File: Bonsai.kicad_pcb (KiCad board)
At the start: 2 copper layers, 348.5 x 165.6 mm, 202 parts, among them J1 AVR-ISP-6, U1 ATmega32A-PU, Y1 Crystal

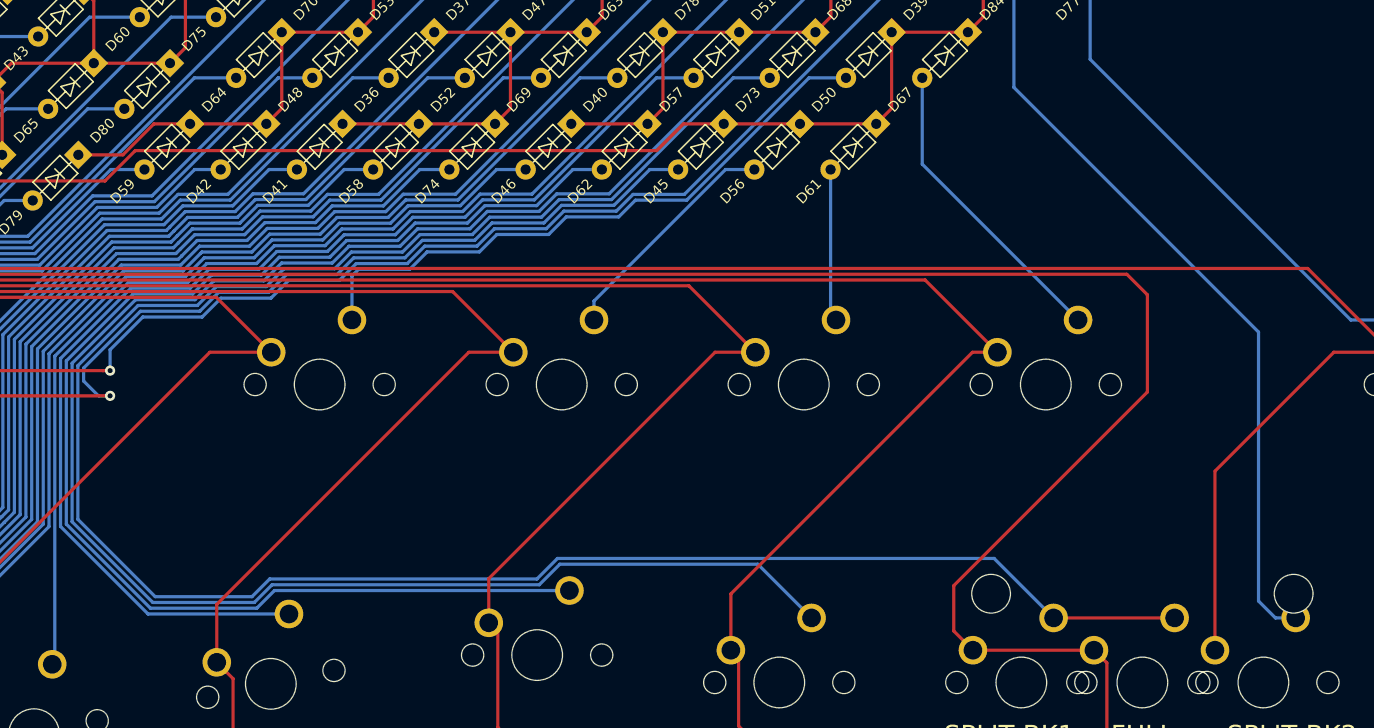
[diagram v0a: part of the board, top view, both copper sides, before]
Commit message: Cleared some space around the backspace stab holes.
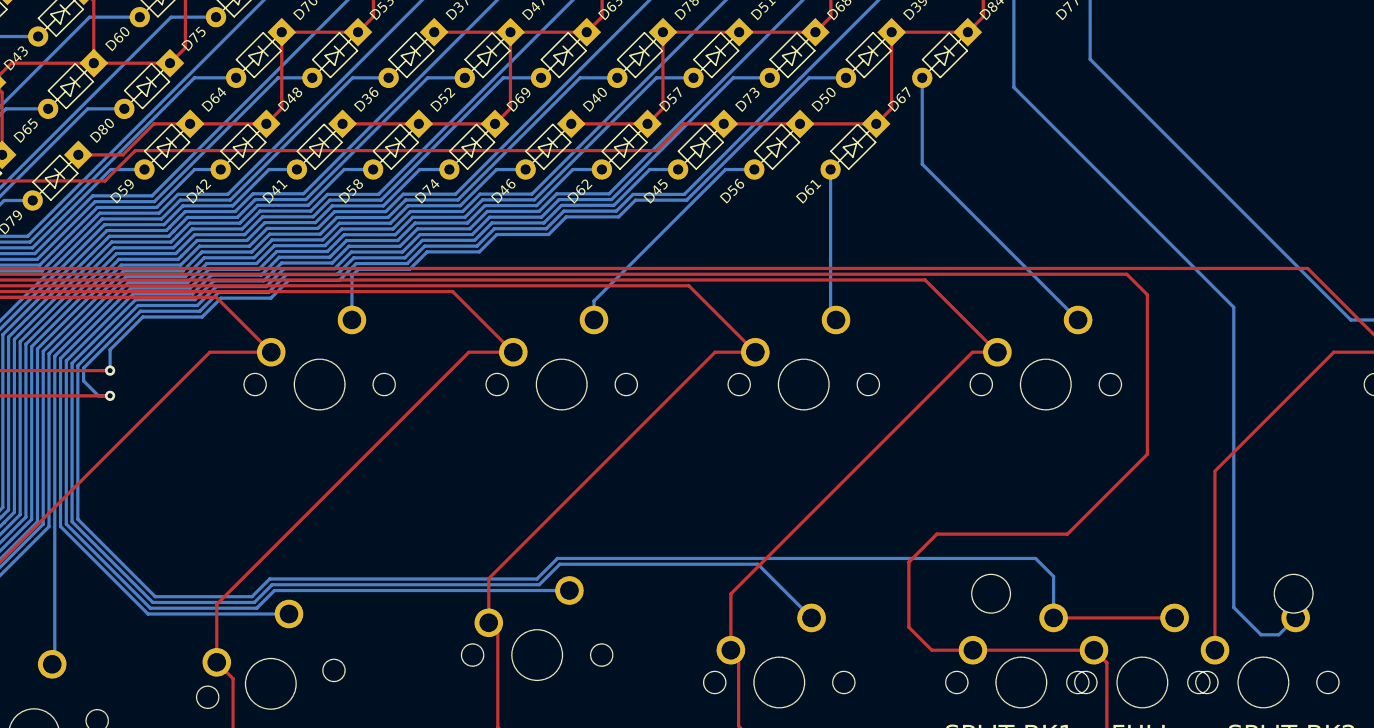
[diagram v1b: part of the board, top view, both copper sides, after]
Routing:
- net col13: track 272.0 -> 282.9 mm
- net Net-(D84-Pad2): track 59.8 -> 62.4 mm
- net Net-(D73-Pad2): track 168.0 -> 169.9 mm

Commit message: Fixed plate, added art to the PCB and made a base plate with art.
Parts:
- added G***: LOGO, Art:Bonsai Back 650x650, B.Cu at (199.2, 157.5)
- added G01: LOGO, Art:Bonsai Front Badge 6k x6k, F.Cu at (338.0, 86.1)
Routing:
- net GND: vias 0 -> 22
